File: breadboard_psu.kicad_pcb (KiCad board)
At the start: 2 copper layers, 55.2 x 71.1 mm, 21 parts, among them J1 Barrel_Jack_MountingPin, J2 Conn_01x02, J3 Conn_01x02, J4 Conn_02x04_Odd_Even, J5 Conn_01x02, SW1 SW_DPDT_x2, SW2 SW_DPDT_x2, U1 LM317_TO-220

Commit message: Alonger les tabs
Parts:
- J3: value Conn_01x02 -> locked
- moved C2 11.5 mm to (126.3, 108.0), turned to 0 degrees
- moved C1 8.07 mm to (128.8, 89.7), turned to 0 degrees
- moved H3 5.33 mm to (132.3, 63.5)
- moved H4 5.33 mm to (132.3, 126.5)
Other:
- outline, holes or cut-outs redrawn

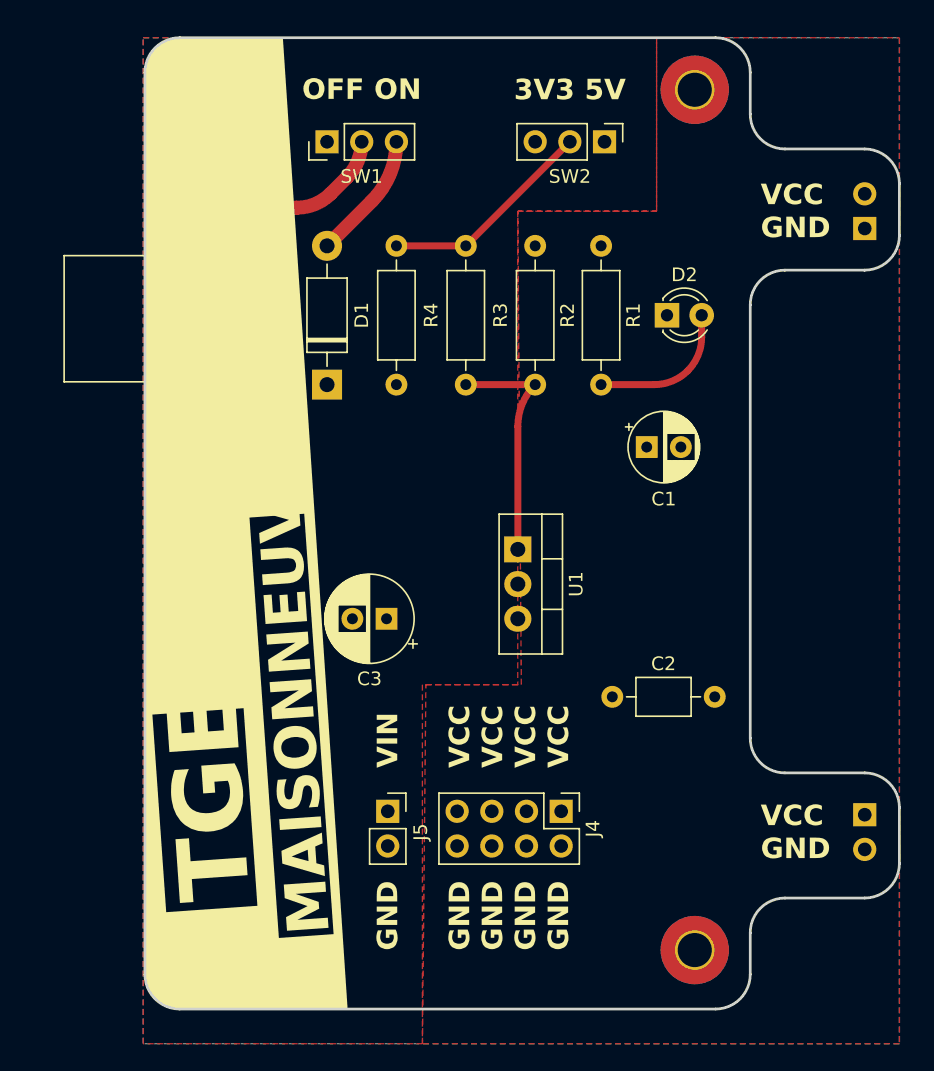
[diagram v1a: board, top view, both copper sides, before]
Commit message: MaJ TO220 a plat + esthétique
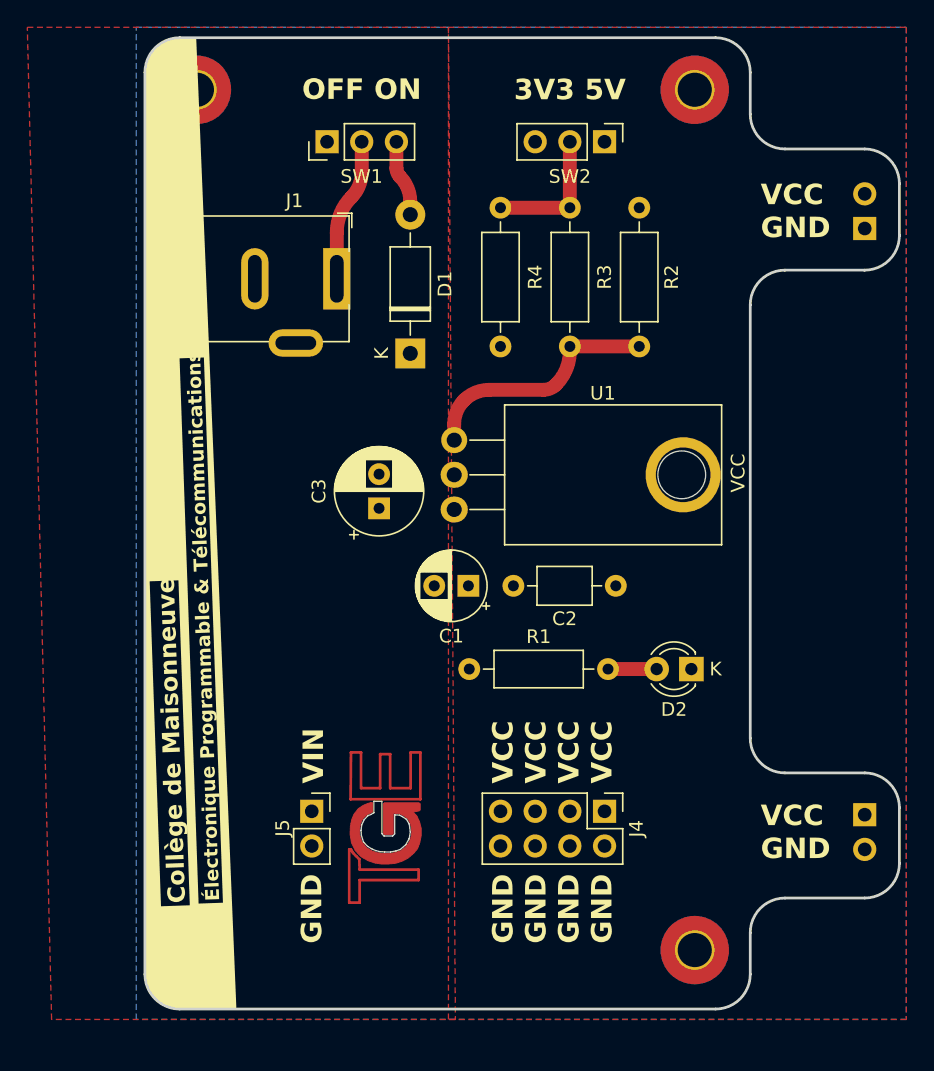
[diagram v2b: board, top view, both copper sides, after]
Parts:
- J1: footprint Connector_BarrelJack:BarrelJack_Kycon_KLDX-0202-xC_Horizontal -> Connector_BarrelJack:BarrelJack_Horizontal_PJ-002A
- U1: footprint Package_TO_SOT_THT:TO-220-3_Vertical -> Package_TO_SOT_THT:TO-220-3_Horizontal_TabDown_Connected
- moved R1 32.5 mm to (115.8, 105.9), turned to 0 degrees
- moved D2 26.0 mm to (132.1, 105.9), turned to 180 degrees
- moved C1 16.5 mm to (115.8, 99.8), turned to 180 degrees
- moved C2 10.9 mm to (119.1, 99.8)
- moved U1 9.26 mm to (114.7, 89.2)
- moved R2 8.12 mm to (128.3, 72.1)
- moved R4 8.12 mm to (118.1, 72.1)
- moved R3 8.12 mm to (123.2, 82.3)
- moved C3 8.11 mm to (109.2, 94.1), turned to 90 degrees
- moved J1 6.62 mm to (106.1, 77.3)
- moved D1 6.51 mm to (111.5, 82.8)
- moved J5 5.56 mm to (104.3, 116.3)
- moved J4 3.17 mm to (125.7, 116.3)
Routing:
- net Net-(D2-A): track 10.9 -> 3.56 mm
- net Net-(SW1A-B): track 17.0 -> 10.5 mm
- net Net-(SW2A-B): track 15.9 -> 9.91 mm
- net Net-(D1-A): track 9.43 -> 5.59 mm
- net Net-(U1-ADJ): track 17.5 -> 18.2 mm
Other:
- outline, holes or cut-outs redrawn
- board text added: "2023"
- board text added: "ALIMENTATION PROTOTYPAGE"
- board text added: "Collège de Maisonneuve"
- board text added: "K"
- board text added: "Nom:"
- board text added: "VCC"
- board text added: "Électronique Programmable & Télécommunications"
- board text removed: "MAISONNEUVE"
- board text removed: "TGE"
